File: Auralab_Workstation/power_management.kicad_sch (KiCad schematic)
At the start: 0 parts

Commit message: Add files via upload
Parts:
- added C1: C, symbol Device:C
- added C2: C_Polarized, symbol Device:C_Polarized
- added C3: 2.2uF, symbol Device:C
- added D1, D2: MBR0520, Diode_SMD:D_SOD-123, symbol Diode:MBR0520
- added F1: Polyfuse, symbol Device:Polyfuse
- added FB1: FerriteBead, symbol Device:FerriteBead
- added J1: USB_C_Receptacle_USB2.0_16P, symbol Connector:USB_C_Receptacle_USB2.0_16P
- added L1, L2: L, symbol Device:L
- added U1: USBLC6-2SC6, Package_TO_SOT_SMD:SOT-23-6, symbol Power_Protection:USBLC6-2SC6
- added U2: AP2112K-3.3, Package_TO_SOT_SMD:SOT-23-5, symbol Regulator_Linear:AP2112K-3.3
- added U3: TPS65131RGE, Package_DFN_QFN:VQFN-24-1EP_4x4mm_P0.5mm_EP2.45x2.45mm_ThermalVias, symbol Regulator_Switching:TPS65131RGE
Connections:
- new net: F1.1, J1.A4 (VBUS), J1.A9 (VBUS), J1.B4 (VBUS), J1.B9 (VBUS)
- new net: C1.2, F1.2, FB1.1, U2.1 (VIN), U2.3 (EN)
- new net: J1.A7 (D-), U1.1 (I/O1)
- new net: J1.A6 (D+), U1.3 (I/O2)
- new net: D1.2 (A), L1.1, U3.7 (BSW)
- new net: D2.1 (K), L2.2, U3.13 (OUTN), U3.14 (OUTN)
- new net +15V_RAW: C2.1, D1.1 (K)
- new net +3V3_DIGITAL: C3.1, U2.5 (VOUT), U3.10 (ENN), U3.8 (ENP)
- new net +5V_ANALOG: FB1.2, L1.2, L2.1, U3.1 (INP), U3.24 (INP), U3.4 (VIN), U3.5 (INN), U3.6 (INN)
- new net -15V_RAW: D2.2 (A)
- new net GND: C1.1, C3.2, J1.A1 (GND), J1.A12 (GND), J1.B1 (GND), J1.B12 (GND), J1.S1 (SHIELD), U1.2 (GND), U2.2 (GND), U3.11 (PSN), U3.2 (PGND), U3.25 (EP), U3.3 (PGND), U3.9 (PSP)
- new net GNDA: C2.2, U3.19 (AGND)
- new net USB_D+: U1.4 (I/O2)
- new net USB_D-: U1.6 (I/O1)

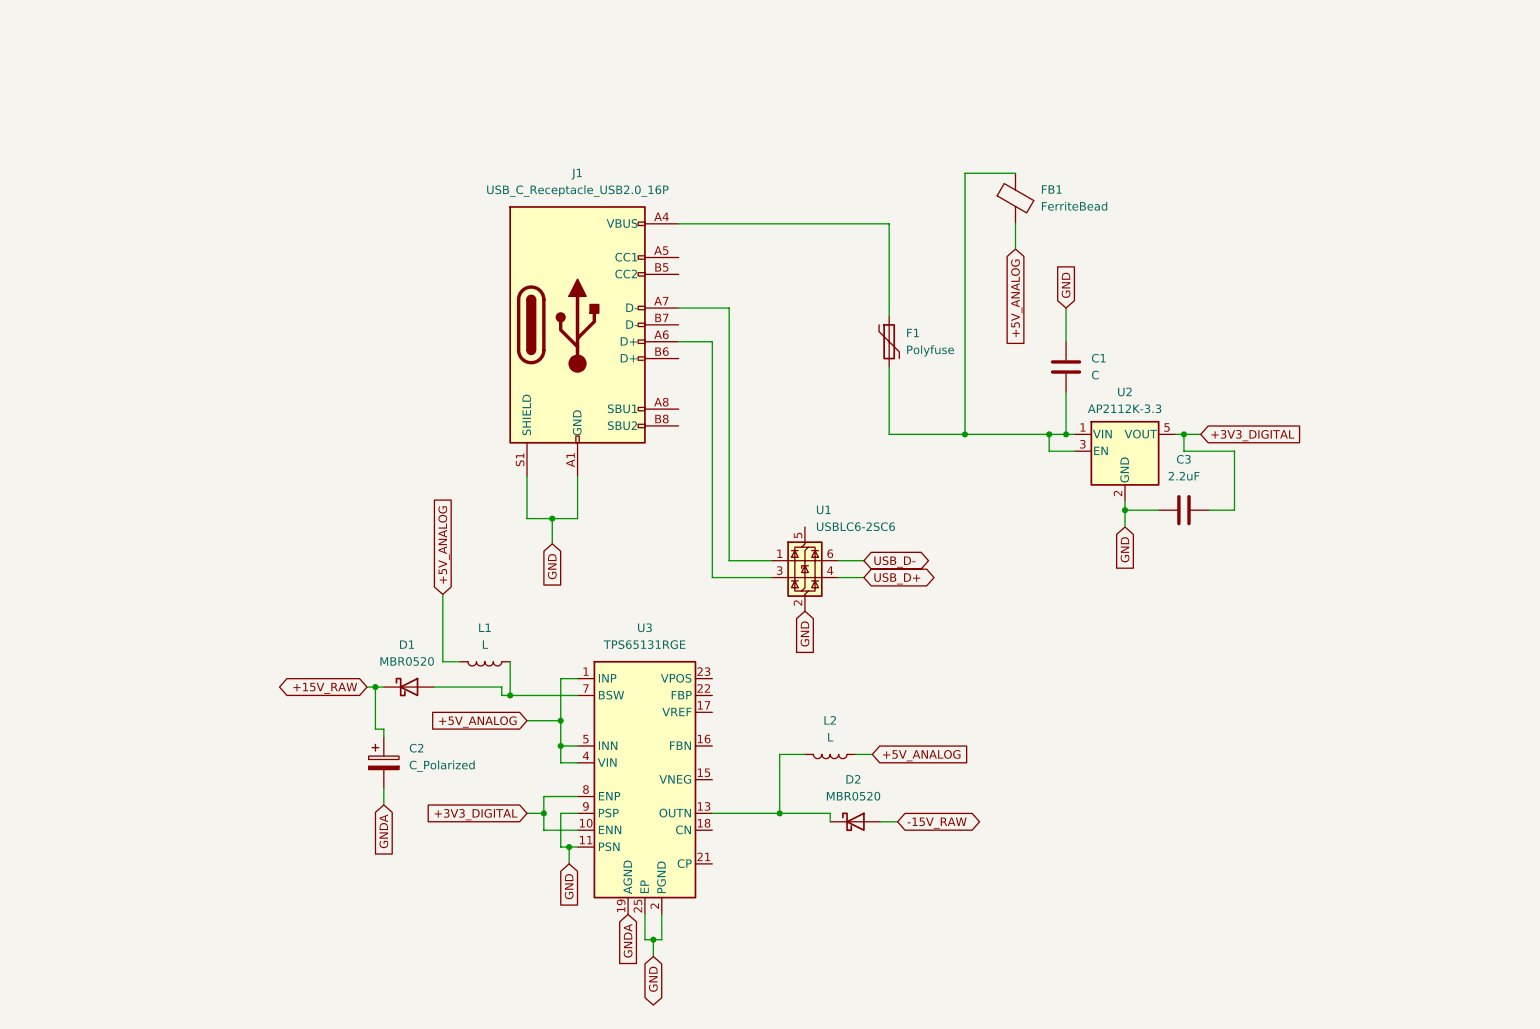
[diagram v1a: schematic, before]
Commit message: Finished power management connections IG
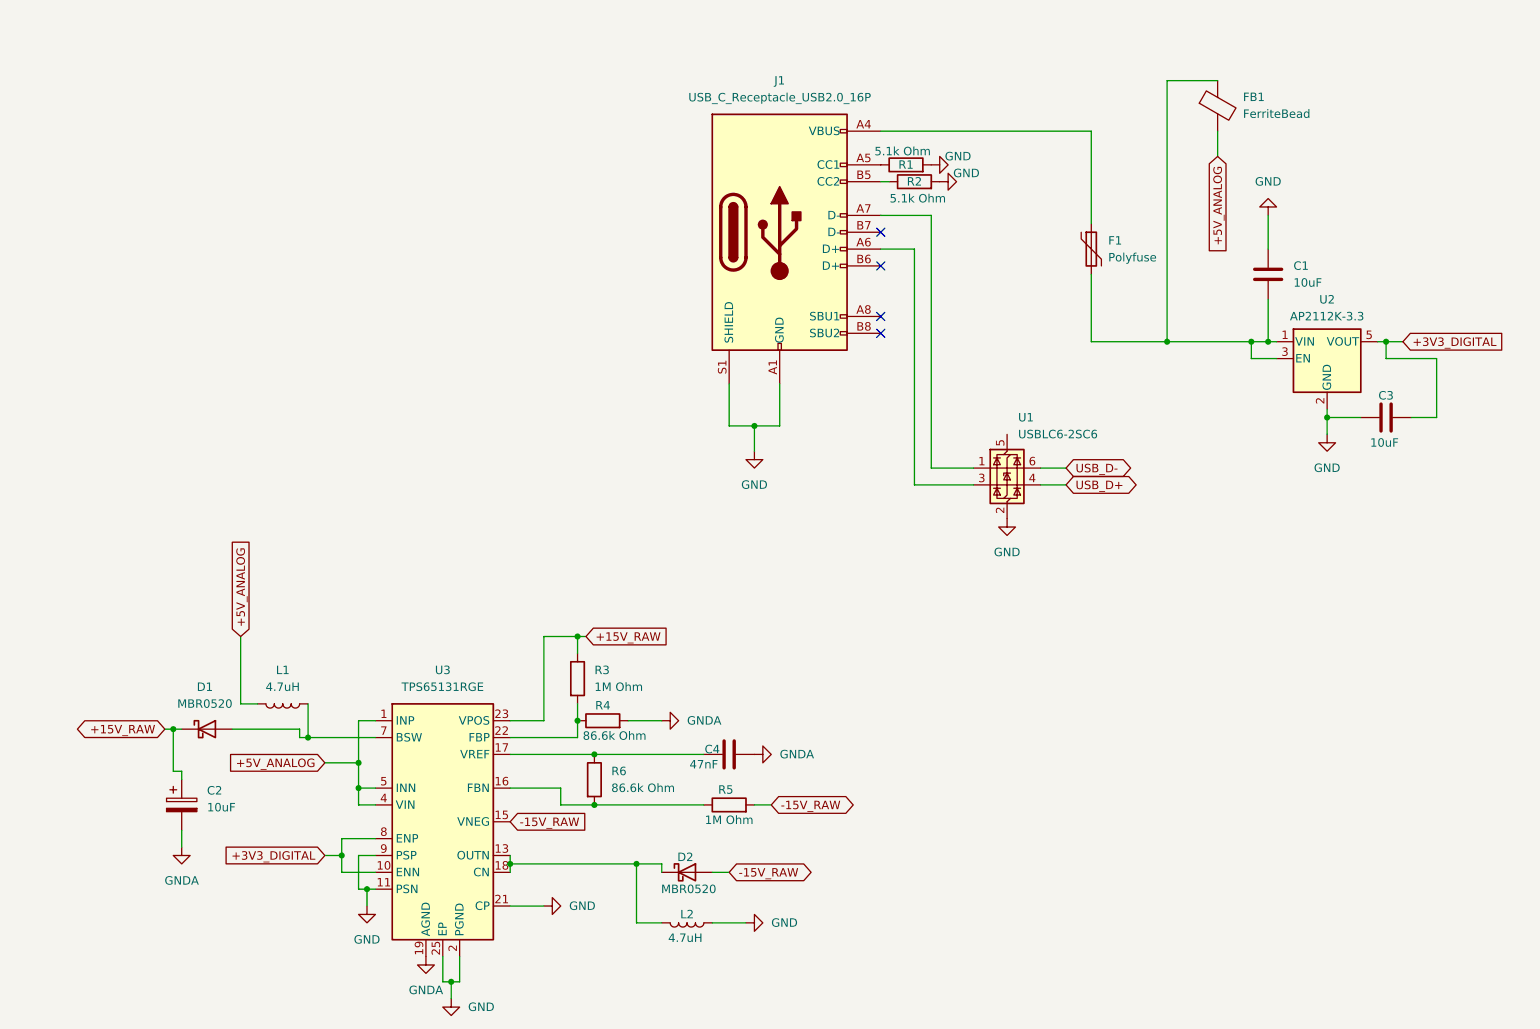
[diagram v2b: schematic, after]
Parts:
- added C4: 47nF, symbol Device:C
- added R1, R2: 5.1k Ohm, symbol Device:R
- added R3, R5: 1M Ohm, symbol Device:R
- added R4, R6: 86.6k Ohm, symbol Device:R
- C1: value C -> 10uF
- C2: value C_Polarized -> 10uF
- C3: value 2.2uF -> 10uF
- L1, L2: value L -> 4.7uH
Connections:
- net +15V_RAW: now also U3.23 (VPOS), R3.1
- net +5V_ANALOG: no longer L2.1
- net -15V_RAW: now also U3.15 (VNEG), R5.2
- net GND: now also L2.1, U3.21 (CP), R1.2, R2.2
- net GNDA: now also C4.2, R4.2
- net at D2.1 (K), L2.2, U3.13 (OUTN)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: now also U3.18 (CN)
- net at U3.16 (FBN): now also R5.1, R6.2
- net at U3.17 (VREF): now also C4.1, R6.1
- net at U3.22 (FBP): now also R3.2, R4.1
- net at J1.A5 (CC1): now also R1.1
- net at J1.B5 (CC2): now also R2.1
- no-connect marks 0 -> 4
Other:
- moved on the sheet: C1, C2, C3, D1, D2, F1, FB1, J1, L1, L2, U1, U2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

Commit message: Power kum footprints added
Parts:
- C1, C3, C4: footprint (none) -> Capacitor_SMD:C_0805_2012Metric_Pad1.18x1.45mm_HandSolder
- C2: footprint (none) -> Capacitor_Tantalum_SMD:CP_EIA-6032-28_Kemet-C_HandSolder
- F1: footprint (none) -> Fuse:Fuse_1206_3216Metric
- FB1: footprint (none) -> Inductor_SMD:L_0805_2012Metric_Pad1.15x1.40mm_HandSolder
- J1: footprint (none) -> Connector_USB:USB_C_Receptacle_HRO_TYPE-C-31-M-12
- L1, L2: footprint (none) -> Inductor_SMD:L_6.3x6.3_H3
- R1, R2, R3, R4, R5, R6: footprint (none) -> Resistor_SMD:R_0805_2012Metric_Pad1.20x1.40mm_HandSolder
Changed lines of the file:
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@@
 			)
 		)
-		(property "Footprint" ""
+		(property "Footprint" "Resistor_SMD:R_0805_2012Metric_Pad1.20x1.40mm_HandSolder"
 			(at 104.902 120.65 90)
 			(effects
@@
 			)
 		)
-		(property "Footprint" ""
+		(property "Footprint" "Fuse:Fuse_1206_3216Metric"
 			(at 185.42 60.96 0)
 			(effects
@@
 			)
 		)
-		(property "Footprint" ""
+		(property "Footprint" "Capacitor_Tantalum_SMD:CP_EIA-6032-28_Kemet-C_HandSolder"
 			(at 47.9552 143.51 0)
 			(effects
@@
 			)
 		)
-		(property "Footprint" ""
+		(property "Footprint" "Capacitor_SMD:C_0805_2012Metric_Pad1.18x1.45mm_HandSolder"
 			(at 133.35 131.1148 0)
 			(effects
@@
 			)
 		)
-		(property "Footprint" ""
+		(property "Footprint" "Resistor_SMD:R_0805_2012Metric_Pad1.20x1.40mm_HandSolder"
 			(at 157.48 47.498 90)
 			(effects
@@
 			)
 		)
-		(property "Footprint" ""
+		(property "Footprint" "Inductor_SMD:L_0805_2012Metric_Pad1.15x1.40mm_HandSolder"
 			(at 201.422 34.29 90)
 			(effects
@@
 			)
 		)
-		(property "Footprint" ""
+		(property "Footprint" "Resistor_SMD:R_0805_2012Metric_Pad1.20x1.40mm_HandSolder"
 			(at 156.21 44.958 90)
 			(effects
@@
 			)
 		)
-		(property "Footprint" ""
+		(property "Footprint" "Resistor_SMD:R_0805_2012Metric_Pad1.20x1.40mm_HandSolder"
 			(at 110.49 128.778 90)
 			(effects
@@
 			)
 		)
-		(property "Footprint" ""
+		(property "Footprint" "Inductor_SMD:L_6.3x6.3_H3"
 			(at 62.23 124.46 0)
 			(effects
@@
 			)
 		)
-		(property "Footprint" ""
+		(property "Footprint" "Inductor_SMD:L_6.3x6.3_H3"
 			(at 123.19 157.48 0)
 			(effects
@@
 			)
 		)
-		(property "Footprint" ""
+		(property "Footprint" "Capacitor_SMD:C_0805_2012Metric_Pad1.18x1.45mm_HandSolder"
 			(at 224.79 82.2452 0)
 			(effects
@@
 			)
 		)
-		(property "Footprint" ""
+		(property "Footprint" "Resistor_SMD:R_0805_2012Metric_Pad1.20x1.40mm_HandSolder"
 			(at 129.54 141.478 90)
 			(effects
@@
 			)
 		)
-		(property "Footprint" ""
+		(property "Footprint" "Connector_USB:USB_C_Receptacle_HRO_TYPE-C-31-M-12"
 			(at 140.97 53.34 0)
 			(effects
@@
 			)
 		)
-		(property "Footprint" ""
+		(property "Footprint" "Capacitor_SMD:C_0805_2012Metric_Pad1.18x1.45mm_HandSolder"
 			(at 211.7852 63.5 0)
 			(effects
@@
 			)
 		)
-		(property "Footprint" ""
+		(property "Footprint" "Resistor_SMD:R_0805_2012Metric_Pad1.20x1.40mm_HandSolder"
 			(at 107.442 135.89 90)
 			(effects

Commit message: Power management le few changes made inum full ah complete panle..
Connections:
- net A4: now reaches F1.1, J1.A4 (VBUS), J1.A9 (VBUS), J1.B4 (VBUS), J1.B9 (VBUS)
- net +5V: now reaches C1.2, F1.2, FB1.1, U2.1 (VIN), U2.3 (EN)
- net A7: now reaches J1.A7 (D-), U1.1 (I/O1)
- net A6: now reaches J1.A6 (D+), U1.3 (I/O2)
- net USB_D+ renamed USB_DP
- net USB_D- renamed USB_DM
- no-connect marks 4 -> 5
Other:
- moved on the sheet: C1, C2, C3, C4, D1, D2, F1, FB1, J1, L1, L2, R1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

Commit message: Power management connections checked its perfect now
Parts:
- added C5: 10uF, Capacitor_SMD:C_0805_2012Metric_Pad1.18x1.45mm_HandSolder, symbol Device:C
- added D3: RED_LED, LED_SMD:LED_0805_2012Metric_Pad1.15x1.40mm_HandSolder, symbol Device:LED
- added D4: GREEN_LED, LED_SMD:LED_0805_2012Metric_Pad1.15x1.40mm_HandSolder, symbol Device:LED
- added D5: MBR0520, Diode_SMD:D_SOD-123, symbol Diode:MBR0520
- added J2: Screw_Terminal_01x03, TerminalBlock:TerminalBlock_MaiXu_MX126-5.0-03P_1x03_P5.00mm, symbol Connector:Screw_Terminal_01x03
- added J3: Conn_01x02_Socket, Connector_JST:JST_PH_B2B-PH-K_1x02_P2.00mm_Vertical, symbol Connector:Conn_01x02_Socket
- added R7: 220 Ohm, Resistor_SMD:R_0805_2012Metric_Pad1.20x1.40mm_HandSolder, symbol Device:R
- added U4: TP4056-42-ESOP8, Package_SO:SOIC-8-1EP_3.9x4.9mm_P1.27mm_EP2.41x3.3mm_ThermalVias, symbol Battery_Management:TP4056-42-ESOP8
- added U5: MCP42010, Package_SO:SOIC-14_3.9x8.7mm_P1.27mm, symbol Potentiometer_Digital:MCP42010
- R4: value 86.6k Ohm -> R_prog = 1.2k
- R6: value 86.6k Ohm -> 220 Ohm
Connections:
- net +3V3_DIGITAL: now also U5.11 (~{RS}), U5.12 (~{SHDN}), U5.14 (VDD)
- net A4: now also D5.2 (A); no longer F1.1
- net GND: now also R4.2, C5.2, J3.2 (Pin_2), U4.1 (TEMP), U4.3 (GND), U4.9 (EPAD)
- net GNDA: now also J2.2 (Pin_2), U5.10 (PB0), U5.4 (VSS); no longer R4.2
- net FBP: now reaches R3.2, U3.22 (FBP)
- net FBP: now also U5.8 (PA0), U5.9 (PW0); no longer R4.1
- net Vref: now reaches C4.1, U3.17 (VREF)
- net Vref: now also U5.7 (PA1); no longer R6.1
- net FBN: now reaches R5.1, U3.16 (FBN)
- net FBN: now also U5.5 (PB1), U5.6 (PW1); no longer R6.2
- net +15V_RAW renamed +Vout
- net +Vout: now also J2.1 (Pin_1)
- net +5V renamed VBUS_SYSTEM
- net VBUS_SYSTEM: now also L1.2, U3.1 (INP), U3.24 (INP), U3.4 (VIN), U3.5 (INN), U3.6 (INN), C5.1, J3.1 (Pin_1), U4.5 (BAT); no longer F1.2, FB1.1
- removed net +5V_ANALOG: FB1.2, L1.2, U3.1 (INP), U3.24 (INP), U3.4 (VIN), U3.5 (INN), U3.6 (INN)
- net -15V_RAW renamed -Vout
- net -Vout: now also J2.3 (Pin_3)
- new net: D5.1 (K), F1.1
- new net: F1.2, FB1.1
- new net: R4.1, U4.2 (PROG)
- new net: D4.1 (K), U4.6 (~{STDBY})
- new net: D3.1 (K), U4.7 (~{CHRG})
- new net: D4.2 (A), R7.2
- new net: D3.2 (A), R6.2
- new net +5V_RAW: FB1.2, R6.1, R7.1, U4.4 (V_{CC}), U4.8 (CE)
- new net POT_SPI_CS: U5.1 (~{CS})
- new net POT_SPI_MOSI: U5.3 (SI)
- new net POT_SPI_SCK: U5.2 (SCK)
- no-connect marks 5 -> 6
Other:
- moved on the sheet: C2, F1, FB1

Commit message: ERC checked
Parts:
- renumbered C2 to C3, C1 to C5, C3 to C6, C5 to C7, D1 to D3, D5 to D4, D2 to D5, D3 to D6, D4 to D7, J1 to J3, J2 to J4, J3 to J5, R3 to R10, R5 to R11, R6 to R12, R7 to R13, R4 to R14, R1 to R8, R2 to R9, U3 to U5, U1 to U6, U2 to U7, U4 to U8, U5 to U9
